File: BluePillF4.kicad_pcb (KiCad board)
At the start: 2 copper layers, 87.2 x 22.9 mm, 200 parts, among them J1 MH20-1, J2 MH20-1, J3 MH_RA4-1, J4 47309-2651, J5 U02-BFD3111B0-009, J6 Conn_Coaxial, Q1 IRLML6402, U1 AP2114HA-3.3TRG1, U2 AP2112K3.3-TRG1, U3 STM32F405RGT6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

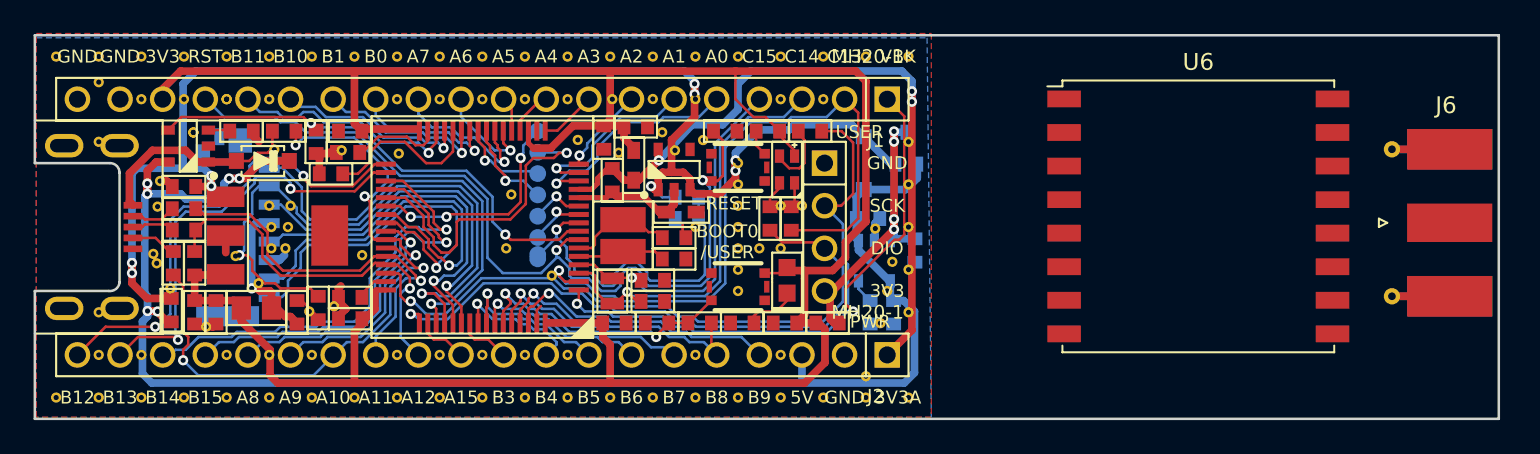
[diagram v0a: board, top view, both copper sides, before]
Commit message: adding 3D shape for Molex 73251-1153 SMA Connector
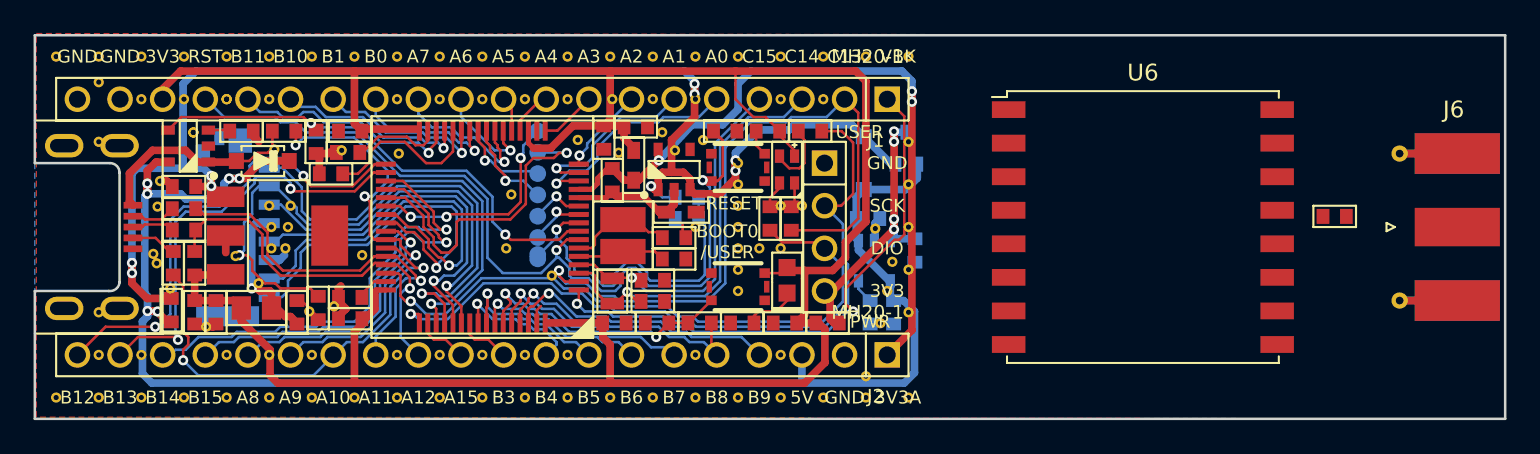
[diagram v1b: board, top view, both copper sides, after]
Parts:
- added C21: 100n, BluePillF4 Lib:C0603, F.Cu at (153.7, 64.1)
- moved U6 3.36 mm to (142.2, 64.8)
- moved J6 0.52 mm to (159.3, 64.8)
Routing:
- net /BluePillF4-1/SDIO_VDD: track 0.00 -> 136.2 mm, vias 0 -> 7
- net /BluePillF4-1/PA11: track 136.2 -> 0.00 mm, vias 7 -> 0
- net /BluePillF4-1/PC13: track 0.00 -> 79.8 mm, vias 0 -> 2
- net /BluePillF4-1/PA13: track 79.8 -> 0.00 mm, vias 2 -> 0
- net /BluePillF4-1/D2_R: track 0.00 -> 3.17 mm
- net /BluePillF4-1/D2_G: track 3.17 -> 0.00 mm
- net GND: track 15.8 -> 17.3 mm
- net /BluePillF4-1/R6: track 1.56 -> 0.00 mm
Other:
- board size 87.2 x 22.9 mm -> 87.6 x 22.9 mm

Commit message: Removed unnecessary components like LiPo charger and fixed most errors. First connections between LoRa module and MCU created in the schematic.
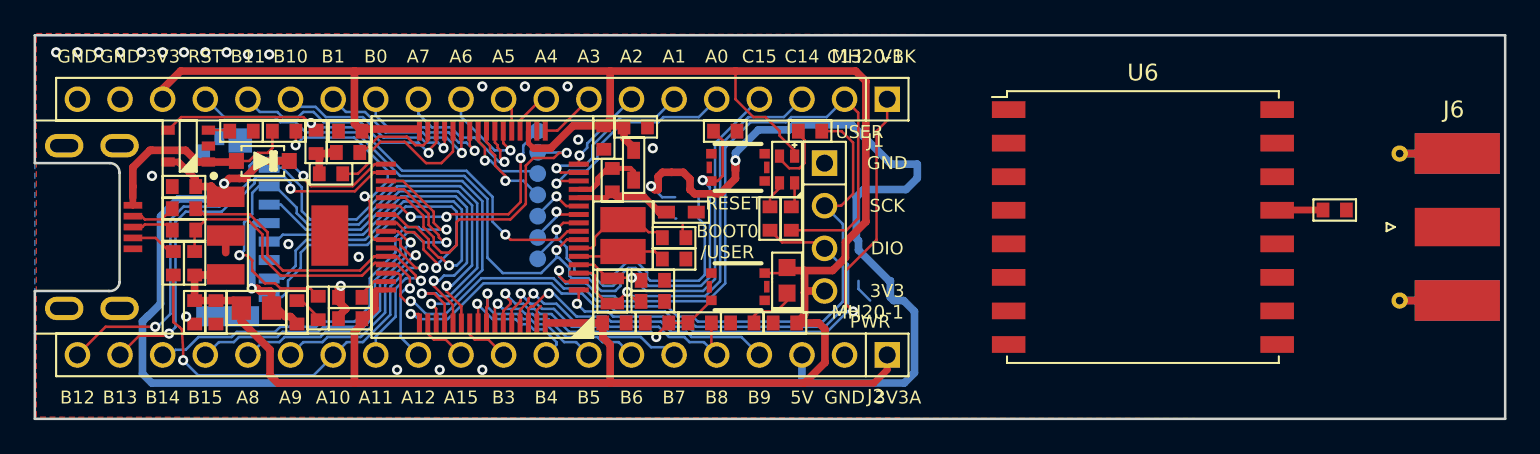
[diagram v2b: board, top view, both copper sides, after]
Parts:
- removed C19, C20: 1u, BluePillF4 Lib:C0603
- removed D4: 1N5819HW, BluePillF4 Lib:SOD-123
- removed PC0: >VALUE, BluePillF4 Lib:TEST_PAD
- removed Q1: IRLML6402, BluePillF4 Lib:SOT323
- removed R17: 15k, BluePillF4 Lib:R0603
- removed R18, R21, R22, R6: 10k, BluePillF4 Lib:R0603
- removed R19, R20: 0R, BluePillF4 Lib:R0603
- removed REF** (x124): VIA_12MIL, BluePillF4 Lib:VIA_12MIL
- removed U$4: , BluePillF4 Lib:OPEN_HARDWARE_LOGO
- removed U$6: , BluePillF4 Lib:RECYCLE_BIN_LOGO
- removed U2: AP2112K3.3-TRG1, BluePillF4 Lib:SOT23-5
- removed U5: MCP73812T-420I/OT, BluePillF4 Lib:SOT23-5
- moved C21 0.38 mm to (153.7, 63.8)
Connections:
- C6 pad 1: +VIN -> +5V
- J1 pad 10: /BluePillF4-1/PA5 -> LoRa_SCK
- J1 pad 11: /BluePillF4-1/PA6 -> LoRa_MISO
- J1 pad 12: /BluePillF4-1/PA7 -> LoRa_MOSI
- J1 pad 9: /BluePillF4-1/PA4 -> LoRa_NSS
- J2 pad 1: +3V3A -> +3V3
- J2 pad 20: PB12 -> /BluePillF4-1/PB12
- J3 pad 4: +VBAT -> +3V3
- U1 pad 1: +VIN -> +5V
- U3 pad 20: /BluePillF4-1/PA4 -> LoRa_NSS
- U3 pad 21: /BluePillF4-1/PA5 -> LoRa_SCK
- U3 pad 22: /BluePillF4-1/PA6 -> LoRa_MISO
- U3 pad 23: /BluePillF4-1/PA7 -> LoRa_MOSI
- U3 pad 33: PB12 -> /BluePillF4-1/PB12
- U6 pad 2: unconnected-(U6-Pad2) -> LoRa_MISO
- U6 pad 3: unconnected-(U6-Pad3) -> LoRa_MOSI
- U6 pad 4: unconnected-(U6-Pad4) -> LoRa_SCK
- U6 pad 5: unconnected-(U6-Pad5) -> LoRa_NSS
- U6 pad 6: PB12 -> unconnected-(U6-Pad6)
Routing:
- net +5V: track 328.4 -> 113.9 mm, vias 28 -> 3
- net /BluePillF4-1/SDIO_VDD: track 136.2 -> 8.74 mm, vias 7 -> 1
- net /BluePillF4-1/PC13: track 79.8 -> 41.1 mm, vias 2 -> 1
- net /BluePillF4-1/PA13: track 0.00 -> 38.8 mm, vias 0 -> 1
- net /BluePillF4-1/SDIO_D3: track 0.00 -> 36.9 mm, vias 0 -> 2
- net /BluePillF4-1/VBK: track 0.00 -> 32.4 mm, vias 0 -> 2
- net /BluePillF4-1/PB12: track 0.00 -> 28.4 mm, vias 0 -> 2
- net /BluePillF4-1/PB13: track 0.00 -> 25.1 mm, vias 0 -> 2
- net /BluePillF4-1/SDIO_D0: track 0.00 -> 23.3 mm, vias 0 -> 1
- net /BluePillF4-1/PA11: track 0.00 -> 23.1 mm, vias 0 -> 1
- net /BluePillF4-1/SDIO_CMD: track 0.00 -> 22.2 mm, vias 0 -> 1
- net /BluePillF4-1/SDIO_CK: track 0.00 -> 21.9 mm, vias 0 -> 1
- net +3V3: track 152.4 -> 163.0 mm
- net LoRa_MOSI: track 0.00 -> 9.30 mm, vias 0 -> 1
- net /BluePillF4-1/PA7: track 9.30 -> 0.00 mm, vias 1 -> 0
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
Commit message: Delete the RTC oscillator. First routing of the LoRa module.
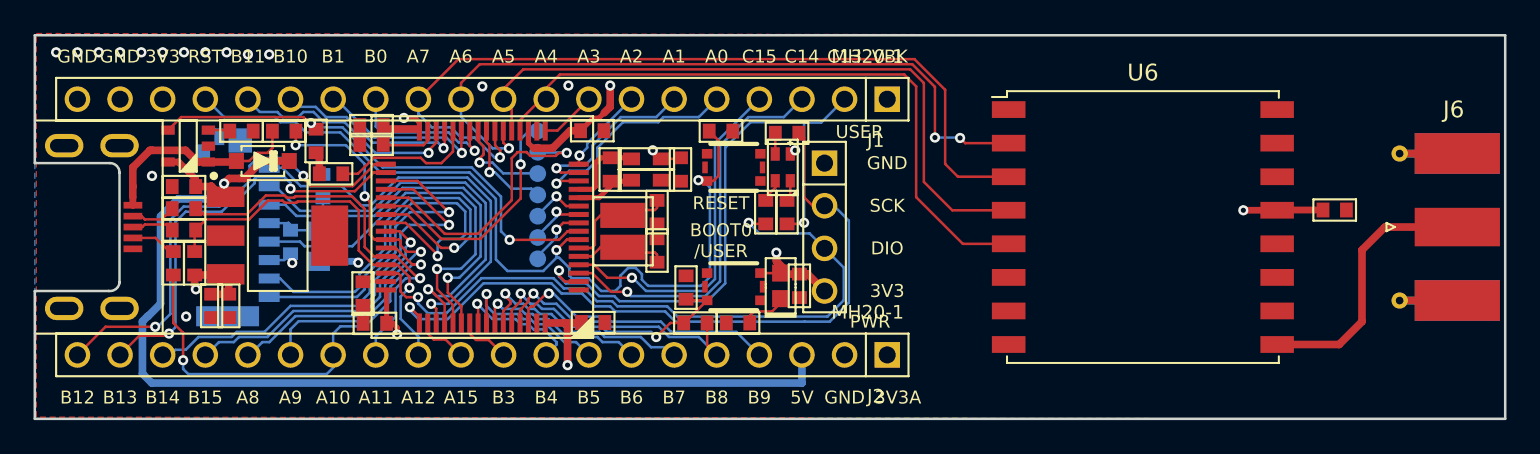
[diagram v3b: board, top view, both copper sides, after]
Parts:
- removed C2, C3: 6p8, BluePillF4 Lib:C0603
- removed Y1: FC-12M, BluePillF4 Lib:FC-12M
- C16, L3, R16: moved to B.Cu
- moved R16 7.27 mm to (93.4, 62.3), turned to 90 degrees
- moved L3 5.21 mm to (93.1, 65.9), turned to -90 degrees
- moved C16 4.21 mm to (91.4, 65.7), turned to 90 degrees
- moved C1 3.68 mm to (114.7, 61.3), turned to -90 degrees
- moved L2 2.82 mm to (112.6, 62.0)
- moved R4 2.73 mm to (115.0, 68.4), turned to 90 degrees
- moved C17 2.37 mm to (121.8, 68.3), turned to 90 degrees
- moved C5 1.83 mm to (113.3, 63.9), turned to -90 degrees
- moved C13 1.50 mm to (96.5, 70.5)
- moved C11 1.48 mm to (96.3, 59.8)
- moved R15 1.38 mm to (121.0, 59.2)
- moved C12 1.31 mm to (96.3, 58.7)
- moved C9 1.27 mm to (109.5, 70.5)
- moved C4 1.14 mm to (113.3, 66.2), turned to 90 degrees
- moved C8 1.09 mm to (86.7, 69.5)
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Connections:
- J1 pad 1: /BluePillF4-1/VBK -> unconnected-(J1-Pad1)
- U3 pad 1: /BluePillF4-1/VBK -> unconnected-(U3-Pad1)
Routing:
- net +3V3: track 163.0 -> 40.7 mm, vias 0 -> 10
- net +5V: track 113.9 -> 65.4 mm, vias 3 -> 1
- net LoRa_MOSI: track 9.30 -> 50.2 mm
- net LoRa_SCK: track 2.07 -> 40.2 mm
- net LoRa_MISO: track 6.17 -> 43.6 mm, vias 1 -> 3
- net LoRa_NSS: track 2.70 -> 39.3 mm
- net /BluePillF4-1/VBK: track 32.4 -> 0.00 mm, vias 2 -> 0
- net /BluePillF4-1/PC1: track 20.8 -> 3.71 mm
- net Net-(J6-Pad1): track 0.00 -> 16.1 mm
- net /BluePillF4-1/SDIO_D3: track 36.9 -> 25.9 mm, vias 2 -> 1
- net GND: track 9.85 -> 2.76 mm, vias 24 -> 16
- net /BluePillF4-1/SDIO_VDD: track 8.74 -> 3.32 mm, vias 1 -> 0
- net /BluePillF4-1/PC13: track 41.1 -> 36.4 mm, vias 1 -> 2
- net /BluePillF4-1/D2_B: track 4.06 -> 1.24 mm
- net AGND: track 6.45 -> 3.91 mm
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- added copper zone on In2.Cu, net +3V3
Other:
- copper layers 2 -> 4

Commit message: Moving some PWR-Nets like 5V to the Bot Layer.
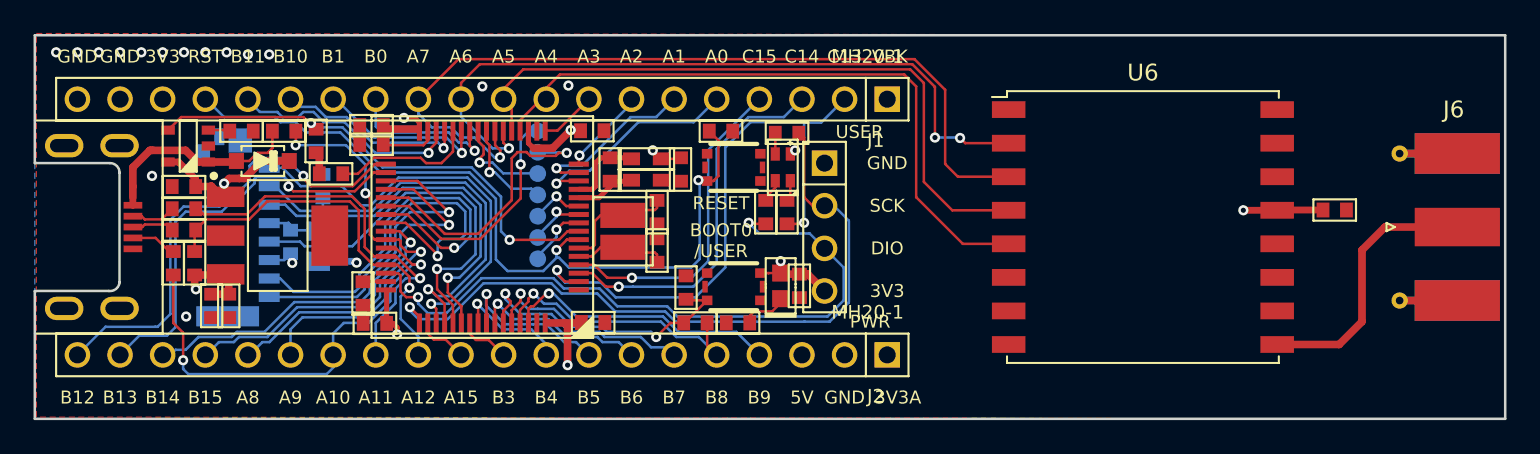
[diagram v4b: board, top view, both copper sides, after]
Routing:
- net +3V3: track 40.7 -> 35.5 mm
- net /BluePillF4-1/NRST: track 51.9 -> 47.6 mm
- net /BluePillF4-1/PC15: track 20.9 -> 19.4 mm
- net /BluePillF4-1/PC14: track 23.5 -> 22.3 mm
- net +5V: track 65.4 -> 64.5 mm
- net /BluePillF4-1/PB4: track 7.88 -> 6.95 mm
- net /BluePillF4-1/PC13: track 36.4 -> 35.8 mm
- net /BluePillF4-1/PB13: vias 2 -> 1
- net /BluePillF4-1/PB12: vias 2 -> 1

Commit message: Added GND at inner level and routed some traces nicely.
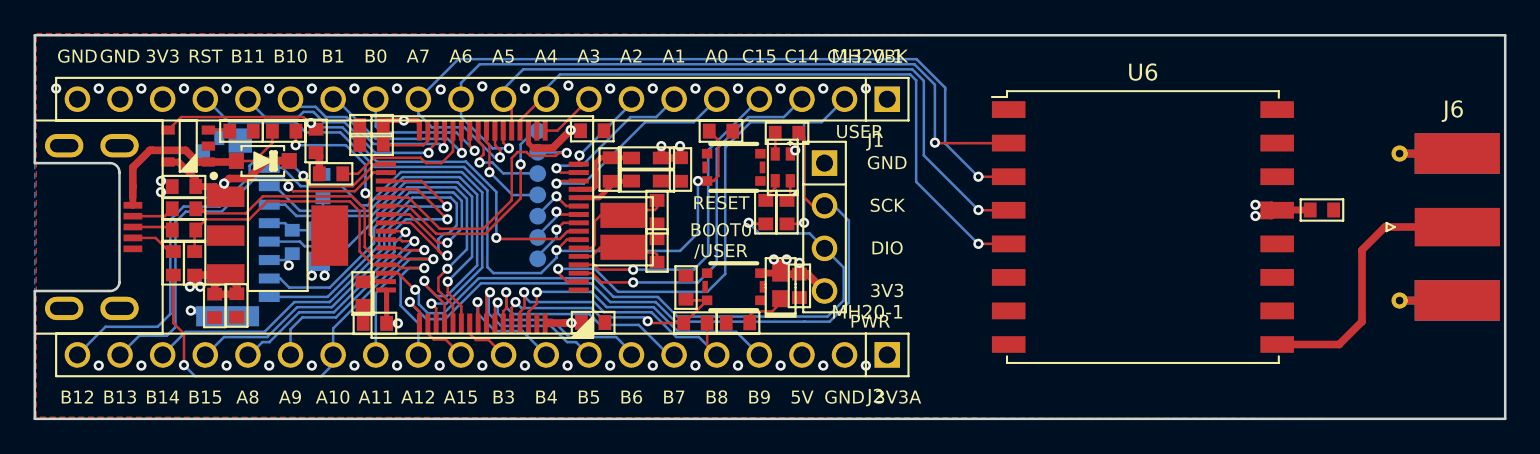
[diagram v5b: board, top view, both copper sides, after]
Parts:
- moved C21 0.76 mm to (152.9, 63.8)
- moved C18 0.48 mm to (88.2, 69.4)
- moved C8 0.18 mm to (86.9, 69.5)
- moved C16 0.10 mm to (91.5, 65.7)
- moved L1 0.05 mm to (112.6, 60.7)
- moved L2 0.05 mm to (112.6, 62.0)
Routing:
- net +5V: track 64.5 -> 74.7 mm
- net GND: track 2.76 -> 5.20 mm, vias 16 -> 42
- net /BluePillF4-1/PA12: track 23.3 -> 25.4 mm
- net /BluePillF4-1/PA11: track 23.5 -> 25.5 mm
- net /BluePillF4-1/SDIO_D0: track 24.0 -> 22.0 mm
- net /BluePillF4-1/BOOT0: track 16.7 -> 15.1 mm
- net /BluePillF4-1/PA9: track 25.1 -> 23.7 mm
- net /BluePillF4-1/PA8: track 15.1 -> 13.9 mm
- net /BluePillF4-1/PB14: track 26.5 -> 25.4 mm
- net +3V3: track 35.5 -> 36.5 mm, vias 10 -> 16
- net /BluePillF4-1/SDIO_CK: track 23.2 -> 22.1 mm
- net /BluePillF4-1/SDIO_D3: track 25.9 -> 26.9 mm
- net /BluePillF4-1/PB15: track 23.6 -> 22.7 mm
- net LoRa_SCK: track 40.2 -> 39.3 mm, vias 0 -> 1
- net /BluePillF4-1/SDIO_D1: track 23.5 -> 22.8 mm
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- added copper zone on In1.Cu, net GND

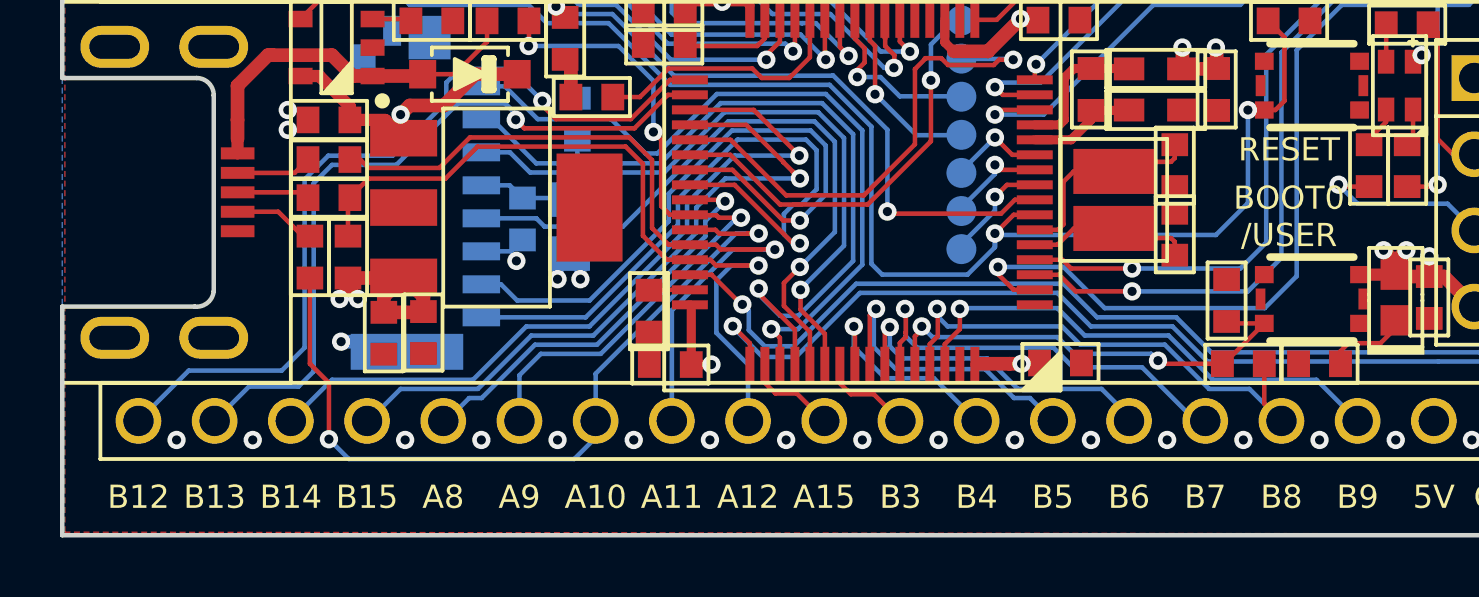
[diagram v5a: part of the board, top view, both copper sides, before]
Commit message: some traces nicely arranged. 3V3 still needs to be made nice (no side connection to MCU)
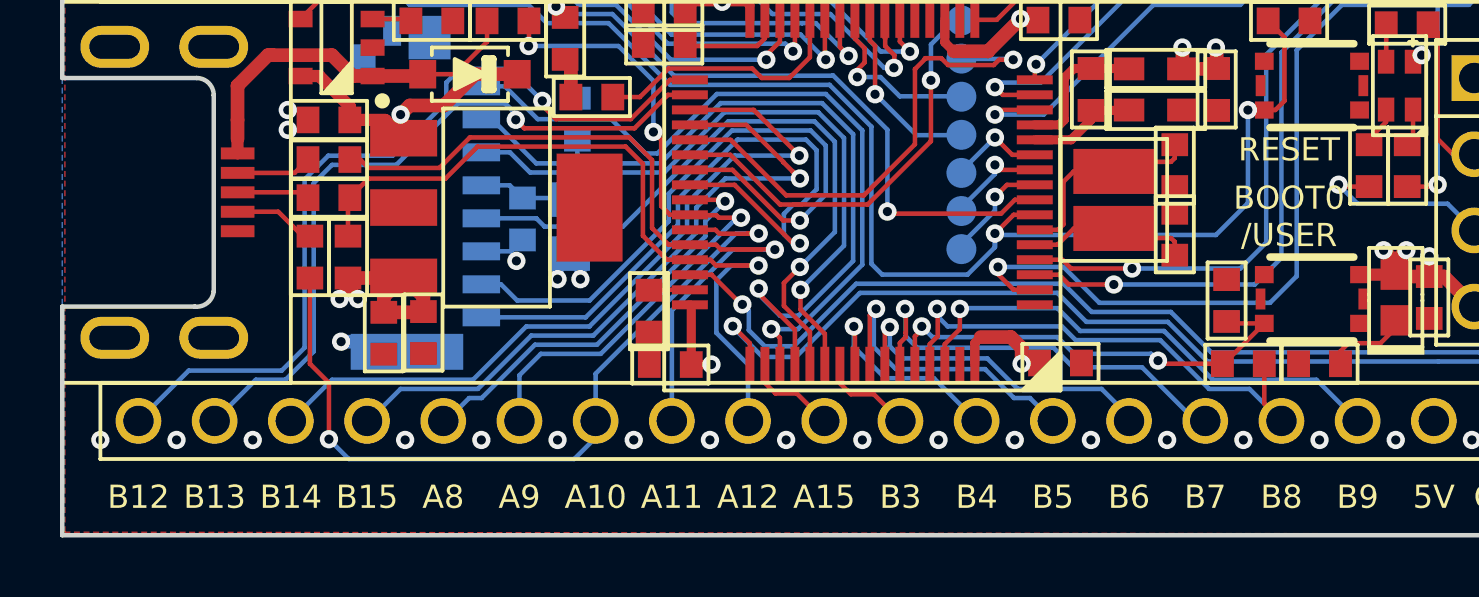
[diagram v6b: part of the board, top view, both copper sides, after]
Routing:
- net +3V3: track 36.5 -> 38.0 mm
- net GND: vias 42 -> 43
